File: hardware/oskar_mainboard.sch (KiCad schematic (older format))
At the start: 5 parts

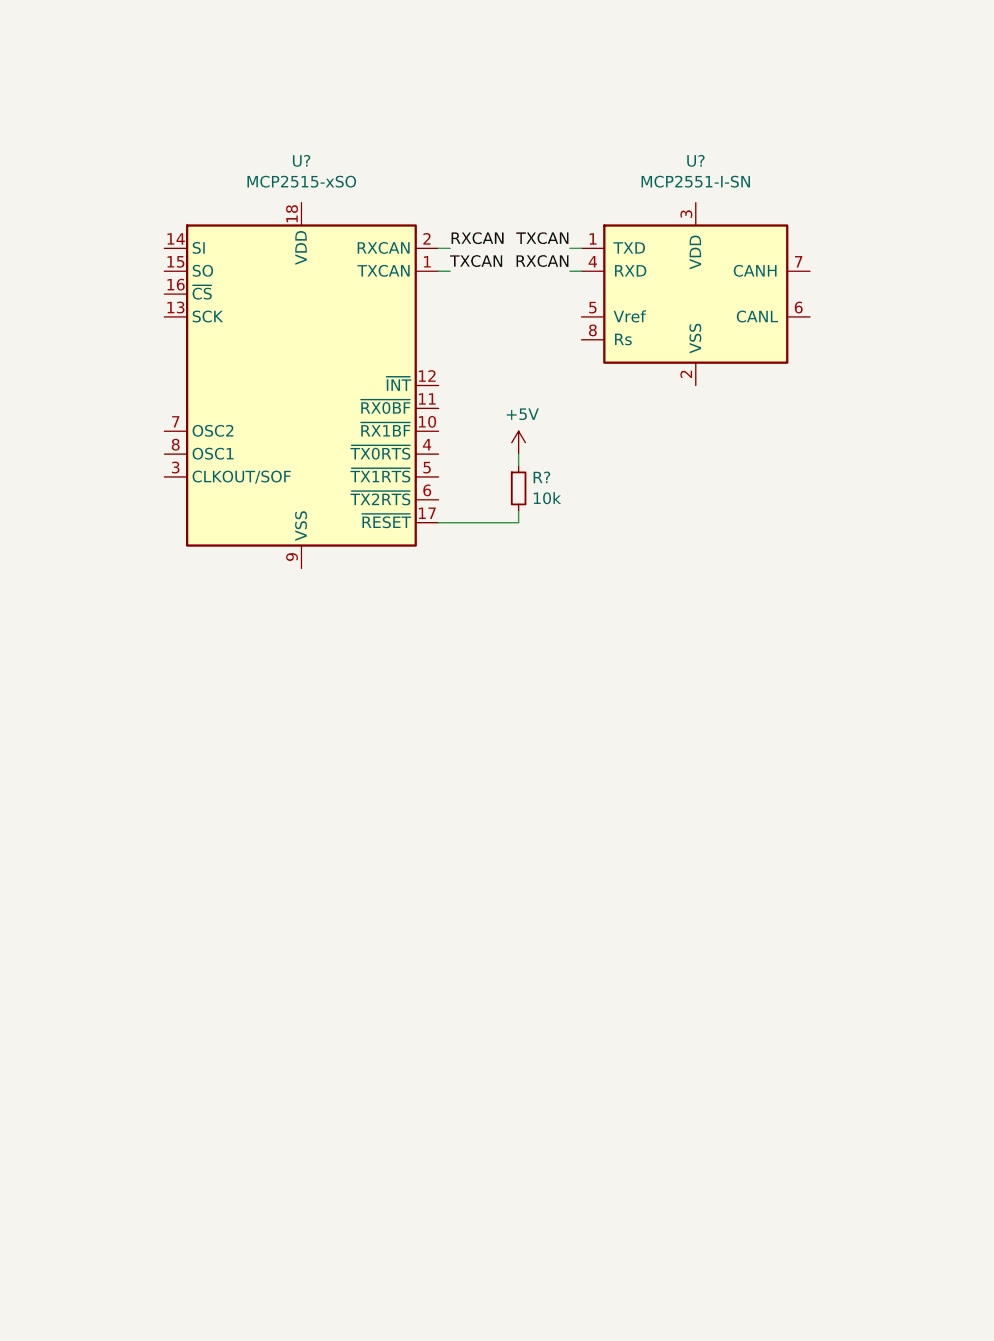
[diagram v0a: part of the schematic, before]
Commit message: Power connections and CAN crystal.
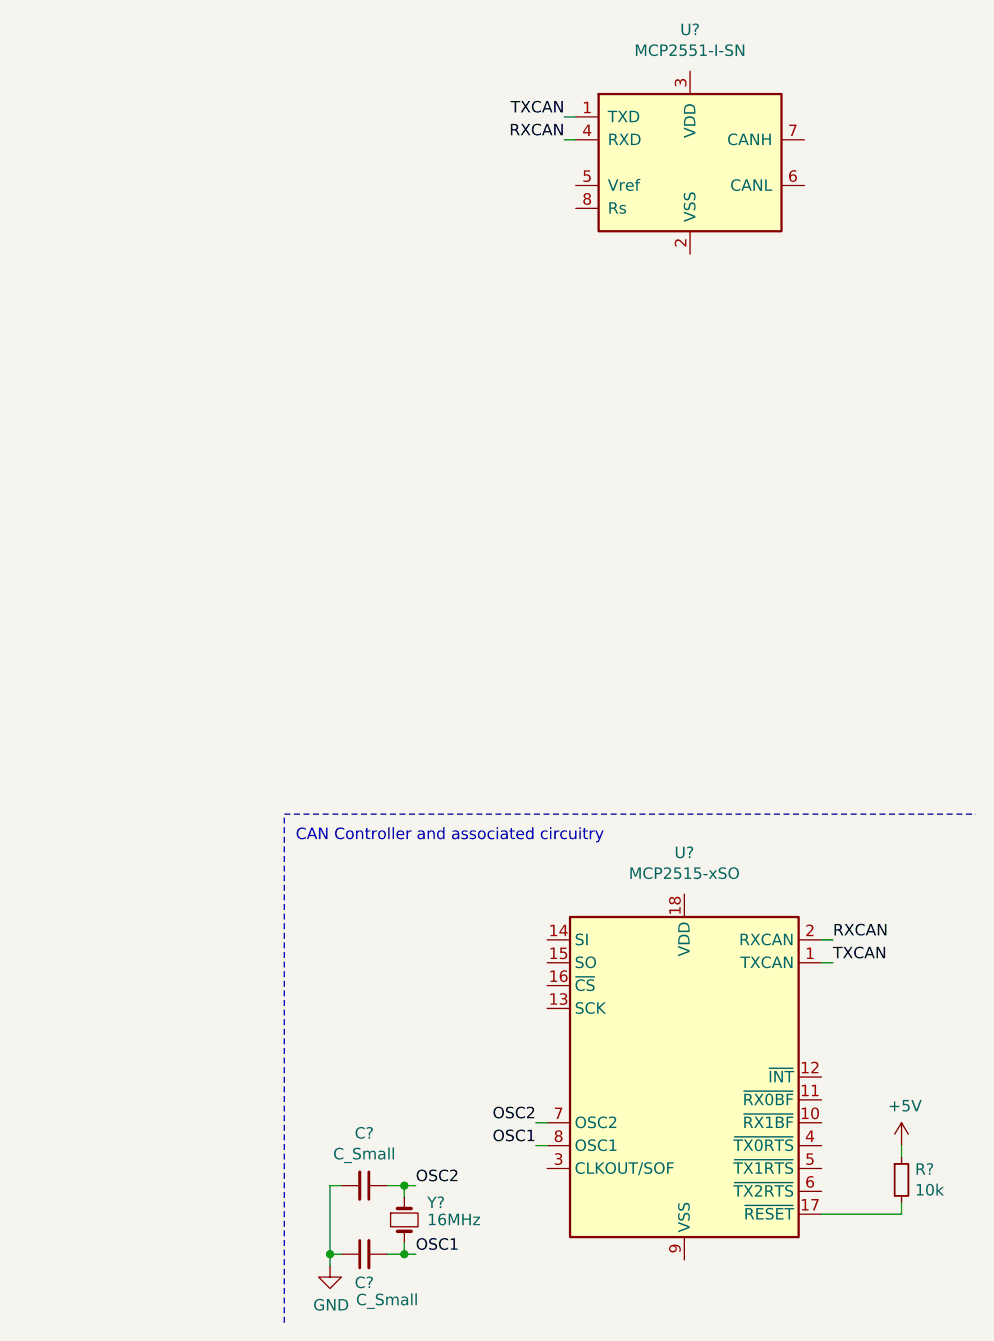
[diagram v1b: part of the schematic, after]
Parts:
- added C? (x2): C_Small, symbol Device:C_Small
- added Y?: 16MHz, symbol Device:Crystal_Small
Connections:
- net GND: now also C?.1, C?.2
- net OSC2: now reaches U?.7 (OSC2)
- net OSC2: now also C?.1, Y?.1
- net OSC1: now reaches U?.8 (OSC1)
- net OSC1: now also C?.2, Y?.2
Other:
- note added: "CAN Controller and associated circuitry"
- moved on the sheet: R?, U?
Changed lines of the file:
@@
 encoding utf-8
 Sheet 1 1
-Title ""
-Date ""
-Rev ""
-Comp ""
-Comment1 ""
+Title "OSKAR III Mainboard"
+Date "2021-01-18"
+Rev "a"
+Comp "Science Centre AHHAA Foundation / SA Teaduskeskus AHHAA"
+Comment1 "Rando Hinn"
 Comment2 ""
 Comment3 ""
@@
 L Interface_CAN_LIN:MCP2515-xSO U?
 U 1 1 60052217
-P 8250 2425
-F 0 "U?" H 8250 3406 50  0000 C CNN
-F 1 "MCP2515-xSO" H 8250 3315 50  0000 C CNN
-F 2 "Package_SO:SOIC-18W_7.5x11.6mm_P1.27mm" H 8250 1525 50  0001 C CIN
-F 3 "http://ww1.microchip.com/downloads/en/DeviceDoc/21801e.pdf" H 8350 1625 50  0001 C CNN
-	1    8250 2425
+P 9925 5450
+F 0 "U?" H 9925 6431 50  0000 C CNN
+F 1 "MCP2515-xSO" H 9925 6340 50  0000 C CNN
+F 2 "Package_SO:SOIC-18W_7.5x11.6mm_P1.27mm" H 9925 4550 50  0001 C CIN
+F 3 "http://ww1.microchip.com/downloads/en/DeviceDoc/21801e.pdf" H 10025 4650 50  0001 C CNN
+	1    9925 5450
 	1    0    0    -1
 $EndComp
@@
 L Interface_CAN_LIN:MCP2551-I-SN U?
 U 1 1 60053ED2
-P 9975 2025
-F 0 "U?" H 9975 2606 50  0000 C CNN
-F 1 "MCP2551-I-SN" H 9975 2515 50  0000 C CNN
-F 2 "Package_SO:SOIC-8_3.9x4.9mm_P1.27mm" H 9975 1525 50  0001 C CIN
-F 3 "http://ww1.microchip.com/downloads/en/devicedoc/21667d.pdf" H 9975 2025 50  0001 C CNN
-	1    9975 2025
-	1    0    0    -1
-$EndComp
-Wire Wire Line
-	8850 1825 8900 1825
-Wire Wire Line
-	9475 1925 9425 1925
-Wire Wire Line
-	9425 1825 9475 1825
-Wire Wire Line
-	8850 1925 8900 1925
-Text Label 8900 1825 0    50   ~ 0
+P 9950 1450
+F 0 "U?" H 9950 2031 50  0000 C CNN
+F 1 "MCP2551-I-SN" H 9950 1940 50  0000 C CNN
+F 2 "Package_SO:SOIC-8_3.9x4.9mm_P1.27mm" H 9950 950 50  0001 C CIN
+F 3 "http://ww1.microchip.com/downloads/en/devicedoc/21667d.pdf" H 9950 1450 50  0001 C CNN
+	1    9950 1450
+	1    0    0    -1
+$EndComp
+Wire Wire Line
+	10525 4850 10575 4850
+Wire Wire Line
+	9450 1350 9400 1350
+Wire Wire Line
+	9400 1250 9450 1250
+Wire Wire Line
+	10525 4950 10575 4950
+Text Label 10575 4850 0    50   ~ 0
 RXCAN
-Text Label 8900 1925 0    50   ~ 0
+Text Label 10575 4950 0    50   ~ 0
 TXCAN
-Text Label 9425 1925 2    50   ~ 0
+Text Label 9400 1350 2    50   ~ 0
 RXCAN
-Text Label 9425 1825 2    50   ~ 0
+Text Label 9400 1250 2    50   ~ 0
 TXCAN
 Wire Wire Line
-	8850 3025 9200 3025
+	10525 6050 10875 6050
 $Comp
 L Device:R_Small R?
 U 1 1 60055B84
-P 9200 2875
-F 0 "R?" H 9259 2921 50  0000 L CNN
-F 1 "10k" H 9259 2830 50  0000 L CNN
-F 2 "Resistor_SMD:R_0603_1608Metric" H 9200 2875 50  0001 C CNN
-F 3 "~" H 9200 2875 50  0001 C CNN
-	1    9200 2875
+P 10875 5900
+F 0 "R?" H 10934 5946 50  0000 L CNN
+F 1 "10k" H 10934 5855 50  0000 L CNN
+F 2 "Resistor_SMD:R_0603_1608Metric" H 10875 5900 50  0001 C CNN
+F 3 "~" H 10875 5900 50  0001 C CNN
+	1    10875 5900
 	1    0    0    -1
 $EndComp
@@
 L power:+5V #PWR?
 U 1 1 60056047
-P 9200 2725
-F 0 "#PWR?" H 9200 2575 50  0001 C CNN
-F 1 "+5V" H 9215 2898 50  0000 C CNN
-F 2 "" H 9200 2725 50  0001 C CNN
-F 3 "" H 9200 2725 50  0001 C CNN
-	1    9200 2725
-	1    0    0    -1
-$EndComp
-Wire Wire Line
-	9200 2725 9200 2775
-Wire Wire Line
-	9200 2975 9200 3025
+P 10875 5750
+F 0 "#PWR?" H 10875 5600 50  0001 C CNN
+F 1 "+5V" H 10890 5923 50  0000 C CNN
+F 2 "" H 10875 5750 50  0001 C CNN
+F 3 "" H 10875 5750 50  0001 C CNN
+	1    10875 5750
+	1    0    0    -1
+$EndComp
+Wire Wire Line
+	10875 5750 10875 5800
+Wire Wire Line
+	10875 6000 10875 6050
 $Comp
 L Device:R_Small R?
@@
 	1    0    0    -1
 $EndComp
+$Comp
+L Device:Crystal_Small Y?
+U 1 1 60058D21
+P 8700 6075
+F 0 "Y?" V 8625 6175 50  0000 L CNN
+F 1 "16MHz" V 8700 6175 50  0000 L CNN
+F 2 "" H 8700 6075 50  0001 C CNN
+F 3 "~" H 8700 6075 50  0001 C CNN
+	1    8700 6075
+	0    1    1    0
+$EndComp
+Wire Wire Line
+	9325 5650 9275 5650
+Wire Wire Line
+	9325 5750 9275 5750
+Text Label 9275 5650 2    50   ~ 0
+OSC2
+Text Label 9275 5750 2    50   ~ 0
+OSC1
+Wire Wire Line
+	8700 5925 8625 5925
+Wire Wire Line
+	8700 5925 8700 5975
+Wire Wire Line
+	8700 6175 8700 6225
+Wire Wire Line
+	8700 6225 8625 6225
+Wire Wire Line
+	8700 5925 8750 5925
+Connection ~ 8700 5925
+Wire Wire Line
+	8700 6225 8750 6225
+Connection ~ 8700 6225
+Text Label 8750 5925 0    50   ~ 0
+OSC2
+Text Label 8750 6225 0    50   ~ 0
+OSC1
+$Comp
+L Device:C_Small C?
+U 1 1 6005B015
+P 8525 5925
+F 0 "C?" V 8296 5925 50  0000 C CNN
+F 1 "C_Small" V 8387 5925 50  0000 C CNN
+F 2 "" H 8525 5925 50  0001 C CNN
+F 3 "~" H 8525 5925 50  0001 C CNN
+	1    8525 5925
+	0    1    1    0
+$EndComp
+$Comp
+L Device:C_Small C?
+U 1 1 6005B0EB
+P 8525 6225
+F 0 "C?" V 8650 6225 50  0000 C CNN
+F 1 "C_Small" V 8725 6125 50  0000 C CNN
+F 2 "" H 8525 6225 50  0001 C CNN
+F 3 "~" H 8525 6225 50  0001 C CNN
+	1    8525 6225
+	0    -1   1    0
+$EndComp
+Wire Wire Line
+	8425 5925 8375 5925
+Wire Wire Line
+	8375 5925 8375 6225
+Wire Wire Line
+	8375 6225 8425 6225
+Wire Wire Line
+	8375 6225 8375 6275
+Connection ~ 8375 6225
+$Comp
+L power:GND #PWR?
+U 1 1 6005C82D
+P 8375 6275
+F 0 "#PWR?" H 8375 6025 50  0001 C CNN
+F 1 "GND" H 8380 6102 50  0000 C CNN
+F 2 "" H 8375 6275 50  0001 C CNN
+F 3 "" H 8375 6275 50  0001 C CNN
+	1    8375 6275
+	1    0    0    -1
+$EndComp
+Wire Notes Line
+	8175 6525 8175 4300
+Wire Notes Line
+	8175 4300 11200 4300
+Text Notes 8225 4425 0    50   ~ 0
+CAN Controller and associated circuitry
 $EndSCHEMATC

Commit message: WIP
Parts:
- removed U?: ATmega2561-16AU, Package_QFP:TQFP-64_14x14mm_P0.8mm, symbol MCU_Microchip_ATmega:ATmega2561-16AU
- added Q1: BC847, Package_TO_SOT_SMD:SOT-23, symbol Transistor_BJT:BC847
- added R3: 1.5k, Resistor_SMD:R_0603_1608Metric, symbol Device:R_Small
- added R4: 10k, Resistor_SMD:R_0603_1608Metric, symbol Device:R_Small
- added U1: ATmega2560-16AU, Package_QFP:TQFP-100_14x14mm_P0.5mm, symbol MCU_Microchip_ATmega:ATmega2560-16AU
- gave numbers to parts that had none: 7
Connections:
- net +5V: now also R4.1
- net GND: now also Q1.2 (E), U1.11 (GND), U1.32 (GND), U1.62 (GND), U1.81 (GND), U1.99 (GND)
- net at R1.1: now also U1.30 (~RESET)
- net CANL: now reaches U3.6 (CANL)
- net CANH: now reaches U3.7 (CANH)
- net OSC1: no longer names the net of C2.2, U2.8 (OSC1), Y1.2
- net OSC2: no longer names the net of C1.1, U2.7 (OSC2), Y1.1
- new net: U1.10 (VCC), U1.31 (VCC), U1.61 (VCC), U1.80 (VCC)
- new net: Q1.1 (B), R3.2
- new net SBUS_CONN: R3.1
- new net SBUS_IN: Q1.3 (C), R4.2
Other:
- note added: "SBUS Inverter"
- moved on the sheet: C1, C2, R1, R2, U2, U3, Y1
